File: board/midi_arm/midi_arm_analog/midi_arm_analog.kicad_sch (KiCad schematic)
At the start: 8 parts, among them U1 LM741

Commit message: analog sim update
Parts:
- R1, R3, R4, R5: value 1500 -> 2400
- R2: value 3900 -> 24000
- R_sense1: value 1400 -> 2400
- U1: value LM741 -> MCP6001
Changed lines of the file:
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@@
       (effects (font (size 1.27 1.27)) (justify left))
     )
-    (property "Value" "1400" (at 113.538 77.4121 0)
+    (property "Value" "2400" (at 113.538 77.4121 0)
       (effects (font (size 1.27 1.27)) (justify left))
     )
@@
       (effects (font (size 1.27 1.27)))
     )
-    (property "Value" "LM741" (at 152.7712 66.733 0)
+    (property "Value" "MCP6001" (at 152.7712 66.733 0)
       (effects (font (size 1.27 1.27)))
     )
@@
       (effects (font (size 1.27 1.27)) hide)
     )
-    (property "Sim.Library" "lm741.lib" (at 143.764 68.326 0)
-      (effects (font (size 1.27 1.27)) hide)
-    )
-    (property "Sim.Name" "LM741" (at 143.764 68.326 0)
+    (property "Sim.Library" "MCP6001.lib" (at 143.764 68.326 0)
+      (effects (font (size 1.27 1.27)) hide)
+    )
+    (property "Sim.Name" "MCP6001" (at 143.764 68.326 0)
       (effects (font (size 1.27 1.27)) hide)
     )
@@
       (effects (font (size 1.27 1.27)) hide)
     )
-    (property "Sim.Pins" "2=2 3=1 4=50 6=28 7=99" (at 143.764 68.326 0)
+    (property "Sim.Pins" "2=2 3=1 4=4 6=5 7=3" (at 143.764 68.326 0)
       (effects (font (size 1.27 1.27)) hide)
     )
@@
   (symbol (lib_id "Device:R") (at 127 82.804 90) (unit 1)
     (in_bom yes) (on_board yes) (dnp no) (fields_autoplaced)
-    (property "Reference" "R1" (at 127 77.6437 90)
-      (effects (font (size 1.27 1.27)))
-    )
-    (property "Value" "1500" (at 127 80.0679 90)
+    (property "Reference" "R1" (at 127 77.47 90)
+      (effects (font (size 1.27 1.27)))
+    )
+    (property "Value" "2400" (at 127 80.01 90)
       (effects (font (size 1.27 1.27)))
     )
@@
   (symbol (lib_id "Device:R") (at 136.144 82.804 90) (unit 1)
     (in_bom yes) (on_board yes) (dnp no) (fields_autoplaced)
-    (property "Reference" "R2" (at 136.144 77.6437 90)
-      (effects (font (size 1.27 1.27)))
-    )
-    (property "Value" "3900" (at 136.144 80.0679 90)
+    (property "Reference" "R2" (at 136.144 77.47 90)
+      (effects (font (size 1.27 1.27)))
+    )
+    (property "Value" "24000" (at 136.144 80.01 90)
       (effects (font (size 1.27 1.27)))
     )
@@
   (symbol (lib_id "Device:R") (at 101.6 66.04 0) (unit 1)
     (in_bom yes) (on_board yes) (dnp no) (fields_autoplaced)
-    (property "Reference" "R4" (at 103.378 64.8279 0)
-      (effects (font (size 1.27 1.27)) (justify left))
-    )
-    (property "Value" "1500" (at 103.378 67.2521 0)
+    (property "Reference" "R4" (at 104.14 64.77 0)
+      (effects (font (size 1.27 1.27)) (justify left))
+    )
+    (property "Value" "2400" (at 104.14 67.31 0)
       (effects (font (size 1.27 1.27)) (justify left))
     )
@@
   (symbol (lib_id "Device:R") (at 101.6 76.2 0) (unit 1)
     (in_bom yes) (on_board yes) (dnp no) (fields_autoplaced)
-    (property "Reference" "R5" (at 103.378 74.9879 0)
-      (effects (font (size 1.27 1.27)) (justify left))
-    )
-    (property "Value" "1500" (at 103.378 77.4121 0)
+    (property "Reference" "R5" (at 104.14 74.93 0)
+      (effects (font (size 1.27 1.27)) (justify left))
+    )
+    (property "Value" "2400" (at 104.14 77.47 0)
       (effects (font (size 1.27 1.27)) (justify left))
     )
@@
   (symbol (lib_id "Device:R") (at 111.76 66.04 0) (unit 1)
     (in_bom yes) (on_board yes) (dnp no) (fields_autoplaced)
-    (property "Reference" "R3" (at 113.538 64.8279 0)
-      (effects (font (size 1.27 1.27)) (justify left))
-    )
-    (property "Value" "1500" (at 113.538 67.2521 0)
-      (effects (font (size 1.27 1.27)) (justify left))
-    )
+    (property "Reference" "R3" (at 114.3 64.77 0)
+      (effects (font (size 1.27 1.27)) (justify left))
+    )
+    (property "Value" "2400" (at 114.3 67.31 0)
+      (effects (font (size 1.27 1.27)) (justify left))
+    )

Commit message: updates
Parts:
- R1, R5: value 2400 -> 3300
- R3: value 2400 -> 5100
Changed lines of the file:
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@@
   (symbol (lib_id "Device:R") (at 127 82.804 90) (unit 1)
     (in_bom yes) (on_board yes) (dnp no) (fields_autoplaced)
-    (property "Reference" "R1" (at 127 77.47 90)
+    (property "Reference" "R1" (at 127 77.6437 90)
       (effects (font (size 1.27 1.27)))
     )
-    (property "Value" "2400" (at 127 80.01 90)
+    (property "Value" "3300" (at 127 80.0679 90)
       (effects (font (size 1.27 1.27)))
     )
@@
   (symbol (lib_id "Device:R") (at 136.144 82.804 90) (unit 1)
     (in_bom yes) (on_board yes) (dnp no) (fields_autoplaced)
-    (property "Reference" "R2" (at 136.144 77.47 90)
+    (property "Reference" "R2" (at 136.144 77.6437 90)
       (effects (font (size 1.27 1.27)))
     )
-    (property "Value" "24000" (at 136.144 80.01 90)
+    (property "Value" "24000" (at 136.144 80.0679 90)
       (effects (font (size 1.27 1.27)))
     )
@@
   (symbol (lib_id "Device:R") (at 101.6 66.04 0) (unit 1)
     (in_bom yes) (on_board yes) (dnp no) (fields_autoplaced)
-    (property "Reference" "R4" (at 104.14 64.77 0)
+    (property "Reference" "R4" (at 103.378 64.8279 0)
       (effects (font (size 1.27 1.27)) (justify left))
     )
-    (property "Value" "2400" (at 104.14 67.31 0)
+    (property "Value" "2400" (at 103.378 67.2521 0)
       (effects (font (size 1.27 1.27)) (justify left))
     )
@@
   (symbol (lib_id "Device:R") (at 101.6 76.2 0) (unit 1)
     (in_bom yes) (on_board yes) (dnp no) (fields_autoplaced)
-    (property "Reference" "R5" (at 104.14 74.93 0)
+    (property "Reference" "R5" (at 103.378 74.9879 0)
       (effects (font (size 1.27 1.27)) (justify left))
     )
-    (property "Value" "2400" (at 104.14 77.47 0)
+    (property "Value" "3300" (at 103.378 77.4121 0)
       (effects (font (size 1.27 1.27)) (justify left))
     )
@@
   (symbol (lib_id "Device:R") (at 111.76 66.04 0) (unit 1)
     (in_bom yes) (on_board yes) (dnp no) (fields_autoplaced)
-    (property "Reference" "R3" (at 114.3 64.77 0)
+    (property "Reference" "R3" (at 113.538 64.8279 0)
       (effects (font (size 1.27 1.27)) (justify left))
     )
-    (property "Value" "2400" (at 114.3 67.31 0)
+    (property "Value" "5100" (at 113.538 67.2521 0)
       (effects (font (size 1.27 1.27)) (justify left))
     )

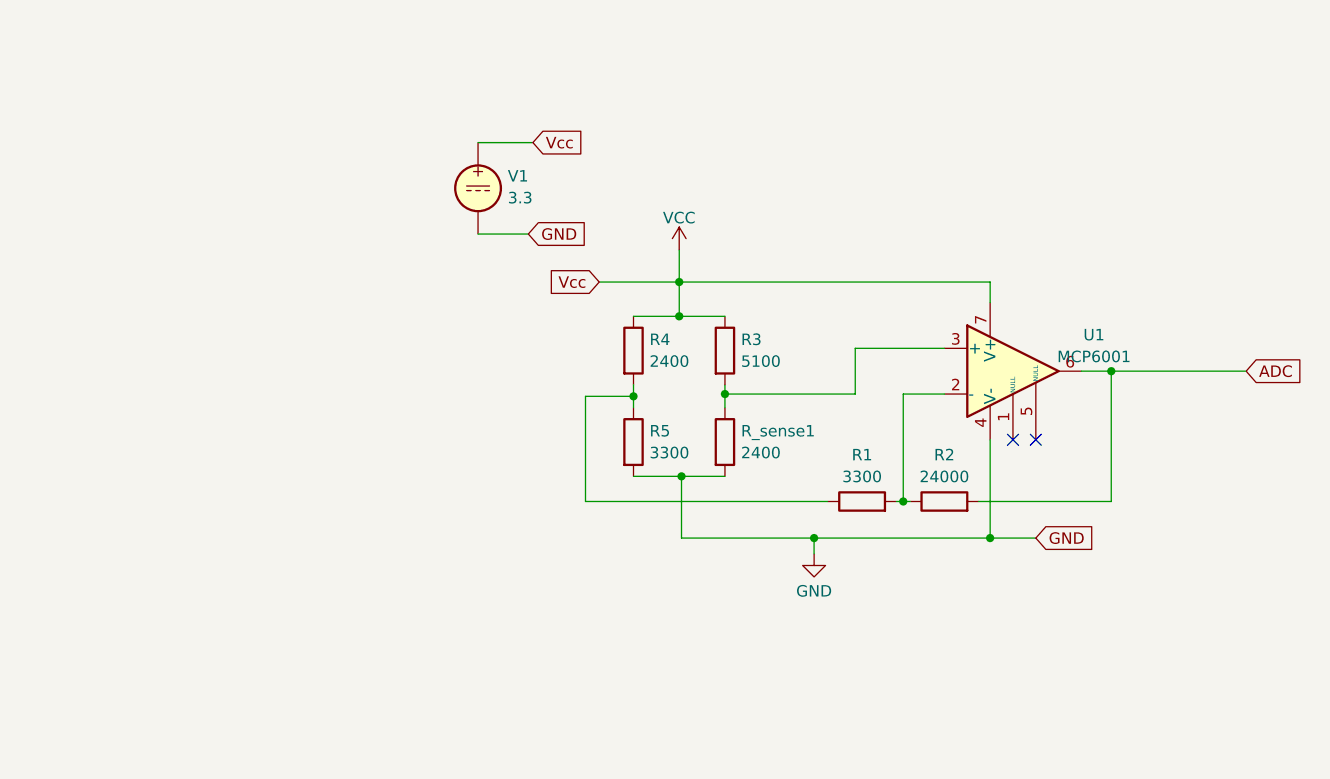
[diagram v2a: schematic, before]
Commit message: HW Version 3 Support
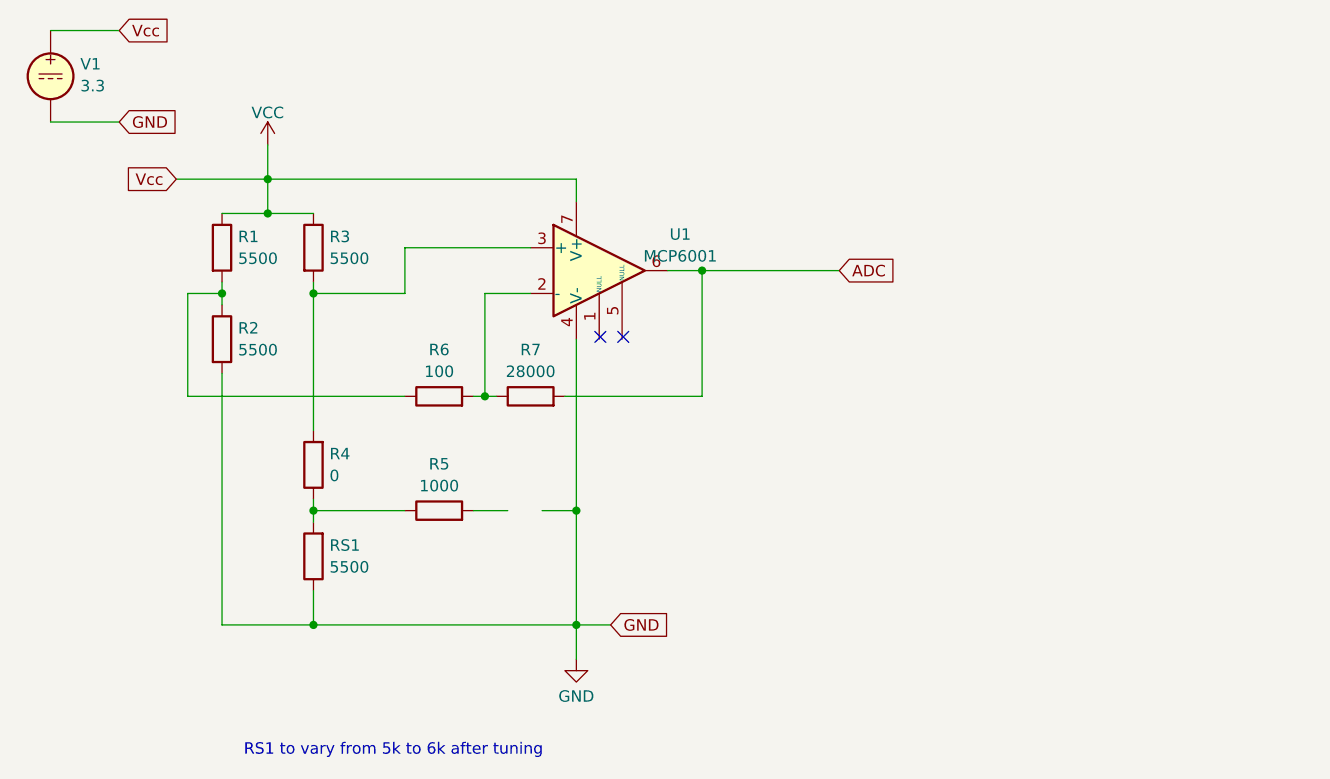
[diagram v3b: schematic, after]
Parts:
- removed R_sense1: 2400, symbol Device:R
- added R4: 0, symbol Device:R
- added R5: 1000, symbol Device:R
- added RS1: 5500, symbol Device:R
- R1: renamed from R4; value 2400 -> 5500
- R2: renamed from R5; value 3300 -> 5500
- R3: value 5100 -> 5500
- R6: renamed from R1; value 3300 -> 100
- R7: renamed from R2; value 24000 -> 28000
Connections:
- net GND: now also RS1.1
- net at R3.2, U1.3 (+): now also R4.2
- new net: R4.1, R5.1, RS1.2
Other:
- note added: "RS1 to vary from 5k to 6k after tuning"
- moved on the sheet: R1, R2, R3, R6, R7, U1, V1

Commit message: Bugfixes
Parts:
- R1, R2, R3: value 5500 -> 33000
- R4: value 0 -> 10000
- R5: value 1000 -> 0
- R6: value 100 -> 0
- R7: value 28000 -> 51000
- RS1: value 5500 -> 15000
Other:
- note added: "RS1 to vary from 10k to 20k after tuning -> Voltage output = 0-1.3V"
- note removed: "RS1 to vary from 5k to 6k after tuning"
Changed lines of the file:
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@@
-	)
-	(junction
-		(at 95.25 83.82)
-		(diameter 0)
-		(color 0 0 0 0)
 	)
 	(junction
@@
 	(wire
 		(pts
-			(xy 83.82 83.82) (xy 87.63 83.82)
-		)
-		(stroke
-			(width 0)
-			(type default)
-		)
-	)
-	(wire
-		(pts
 			(xy 52.07 71.12) (xy 76.2 71.12)
 		)
@@
 	(wire
 		(pts
-			(xy 95.25 83.82) (xy 95.25 96.52)
-		)
-		(stroke
-			(width 0)
-			(type default)
-		)
-	)
-	(wire
-		(pts
 			(xy 109.22 57.15) (xy 124.46 57.15)
 		)
@@
 	(wire
 		(pts
-			(xy 91.44 83.82) (xy 95.25 83.82)
-		)
-		(stroke
-			(width 0)
-			(type default)
-		)
-	)
-	(wire
-		(pts
 			(xy 55.88 96.52) (xy 66.04 96.52)
 		)
@@
 	(wire
 		(pts
-			(xy 95.25 64.77) (xy 95.25 83.82)
+			(xy 95.25 64.77) (xy 95.25 96.52)
 		)
 		(stroke
@@
 		)
 	)
-	(text "RS1 to vary from 5k to 6k after tuning"
+	(text "RS1 to vary from 10k to 20k after tuning -> Voltage output = 0-1.3V"
 		(exclude_from_sim no)
 		(at 74.93 110.49 0)
@@
 			)
 		)
-		(property "Value" "1000"
+		(property "Value" "0"
 			(at 80.01 81.0838 90)
 			(effects
@@
 			)
 		)
-		(property "Value" "100"
+		(property "Value" "0"
 			(at 80.01 68.3838 90)
 			(effects
@@
 			)
 		)
-		(property "Value" "0"
+		(property "Value" "10000"
 			(at 67.818 79.9521 0)
 			(effects
@@
 			)
 		)
-		(property "Value" "28000"
+		(property "Value" "51000"
 			(at 90.17 68.3838 90)
 			(effects
@@
 			)
 		)
-		(property "Value" "5500"
+		(property "Value" "33000"
 			(at 57.658 55.8221 0)
 			(effects
@@
 			)
 		)
-		(property "Value" "5500"
+		(property "Value" "15000"
 			(at 67.818 90.1121 0)
 			(effects
@@
 			)
 		)
-		(property "Value" "5500"
+		(property "Value" "33000"
 			(at 57.658 65.9821 0)
 			(effects
@@
 			)
 		)
-		(property "Value" "5500"
+		(property "Value" "33000"
 			(at 67.818 55.8221 0)
 			(effects

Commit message: Board 3.5 and code cleanup
Mini version of Baboi
Remove Tension Strip option 3/4
Remove  Option for Touch pads
Move light control to host software
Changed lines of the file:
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@@
 		(fields_autoplaced yes)
 		(property "Reference" "V1"
-			(at 40.132 34.2181 0)
+			(at 40.132 34.218 0)
 			(effects
 				(font

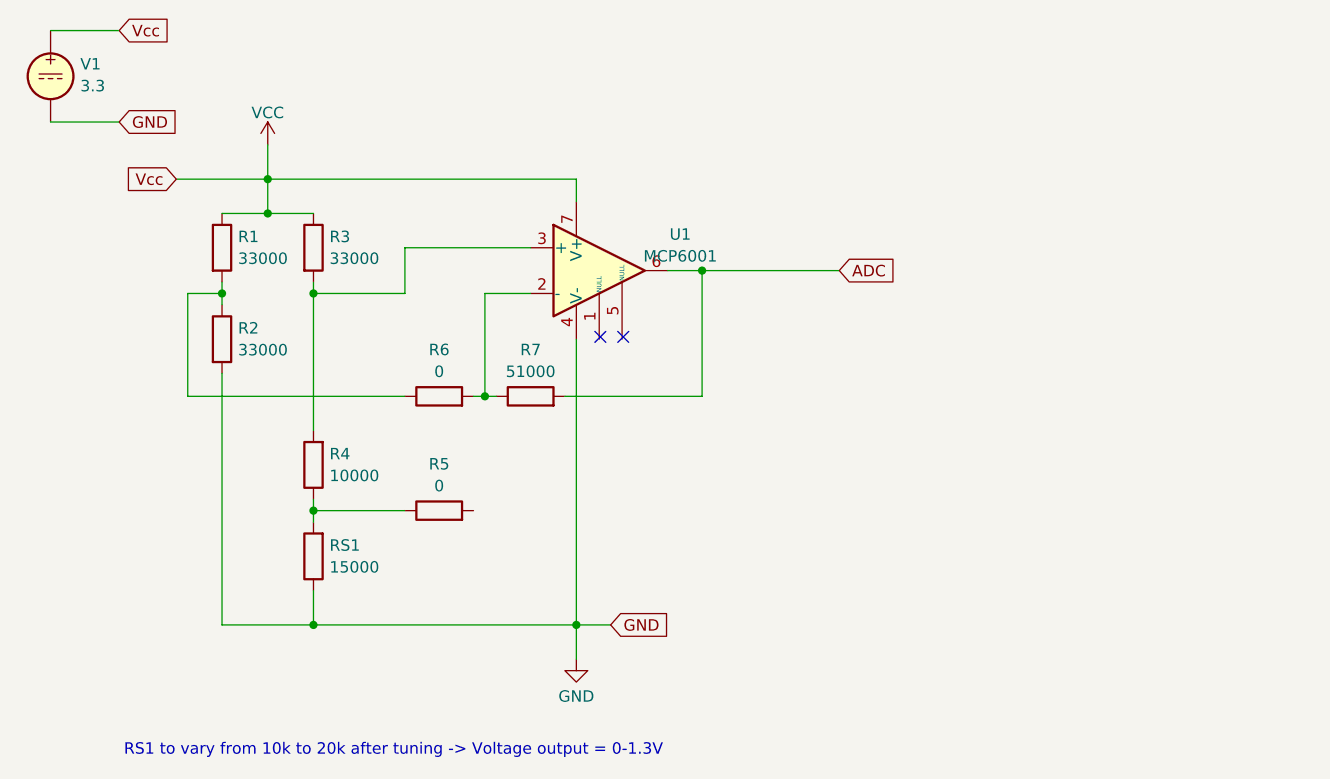
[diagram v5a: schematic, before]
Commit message: Add Led FX, absolute direction calibration, Arrow 3D
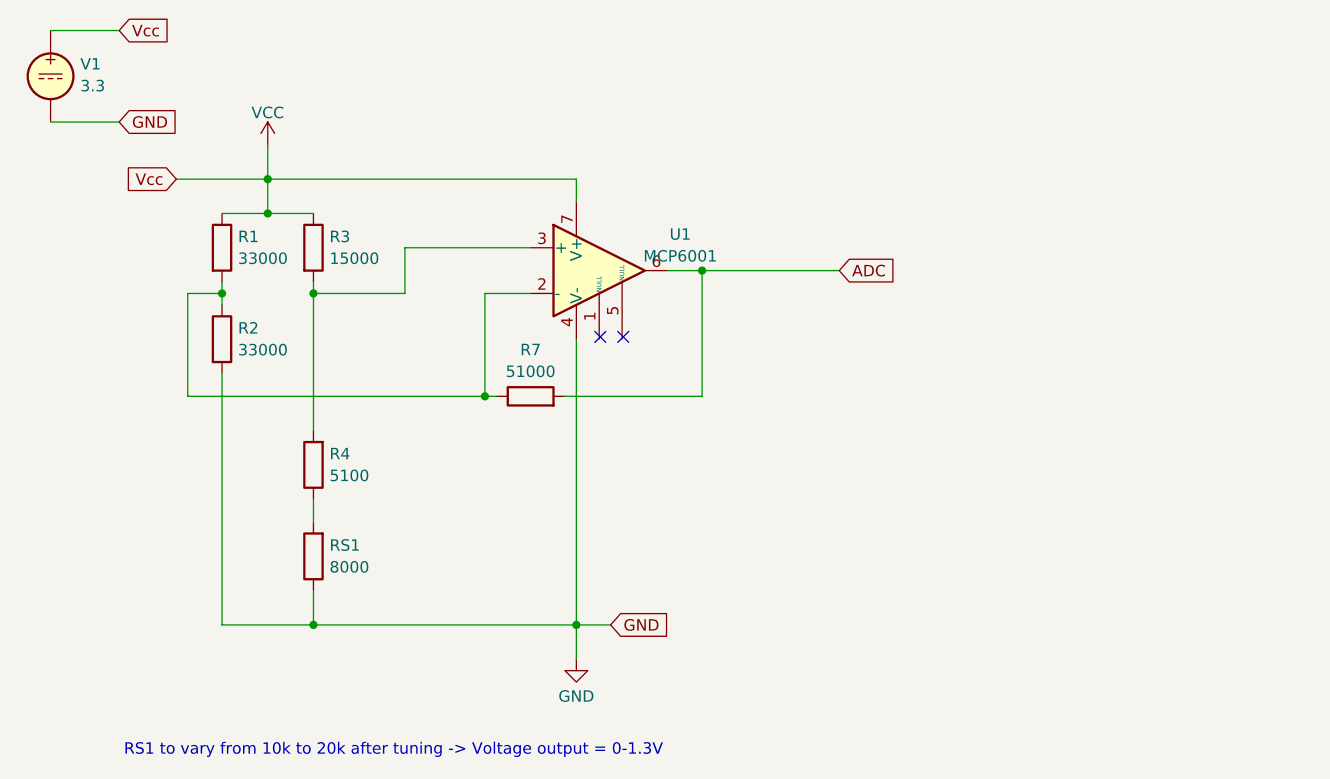
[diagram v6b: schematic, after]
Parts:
- removed R5, R6: 0, symbol Device:R
- R3: value 33000 -> 15000
- R4: value 10000 -> 5100
- RS1: value 15000 -> 8000
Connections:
- net at R7.1, U1.2 (-): now also R1.2, R2.1
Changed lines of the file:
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@@
-	)
-	(junction
-		(at 66.04 83.82)
-		(diameter 0)
-		(color 0 0 0 0)
 	)
 	(junction
@@
 	(wire
 		(pts
-			(xy 52.07 71.12) (xy 76.2 71.12)
+			(xy 52.07 71.12) (xy 85.09 71.12)
 		)
 		(stroke
@@
 	(wire
 		(pts
-			(xy 83.82 71.12) (xy 85.09 71.12)
-		)
-		(stroke
-			(width 0)
-			(type default)
-		)
-	)
-	(wire
-		(pts
 			(xy 109.22 57.15) (xy 124.46 57.15)
 		)
@@
 	(wire
 		(pts
-			(xy 66.04 82.55) (xy 66.04 83.82)
-		)
-		(stroke
-			(width 0)
-			(type default)
-		)
-	)
-	(wire
-		(pts
 			(xy 95.25 64.77) (xy 95.25 96.52)
 		)
@@
 	(wire
 		(pts
-			(xy 66.04 83.82) (xy 76.2 83.82)
-		)
-		(stroke
-			(width 0)
-			(type default)
-		)
-	)
-	(wire
-		(pts
 			(xy 60.96 46.99) (xy 60.96 50.8)
 		)
@@
 	(wire
 		(pts
-			(xy 66.04 83.82) (xy 66.04 85.09)
+			(xy 66.04 82.55) (xy 66.04 85.09)
 		)
 		(stroke
@@
 	)
 	(symbol
-		(lib_id "Device:R")
-		(at 80.01 83.82 90)
-		(unit 1)
-		(exclude_from_sim no)
-		(in_bom yes)
-		(on_board yes)
-		(dnp no)
-		(fields_autoplaced yes)
-		(property "Reference" "R5"
-			(at 80.01 78.6595 90)
-			(effects
-				(font
-					(size 1.27 1.27)
-				)
-			)
-		)
-		(property "Value" "0"
-			(at 80.01 81.0838 90)
-			(effects
-				(font
-					(size 1.27 1.27)
-				)
-			)
-		)
-		(property "Footprint" ""
-			(at 80.01 85.598 90)
-			(effects
-				(font
-					(size 1.27 1.27)
-				)
-				(hide yes)
-			)
-		)
-		(property "Datasheet" "~"
-			(at 80.01 83.82 0)
-			(effects
-				(font
-					(size 1.27 1.27)
-				)
-				(hide yes)
-			)
-		)
-		(property "Description" ""
-			(at 80.01 83.82 0)
-			(effects
-				(font
-					(size 1.27 1.27)
-				)
-				(hide yes)
-			)
-		)
-		(pin "1"
-		)
-		(pin "2"
-		)
-		(instances
-			(project "midi_arm_analog"
-				(path "/307ce423-bb1b-4eb8-9c81-09800713e2e7"
-					(reference "R5")
-					(unit 1)
-				)
-			)
-		)
-	)
-	(symbol
 		(lib_id "Amplifier_Operational:LM741")
 		(at 97.79 57.15 0)
@@
 				(path "/307ce423-bb1b-4eb8-9c81-09800713e2e7"
 					(reference "U1")
-					(unit 1)
-				)
-			)
-		)
-	)
-	(symbol
-		(lib_id "Device:R")
-		(at 80.01 71.12 90)
-		(unit 1)
-		(exclude_from_sim no)
-		(in_bom yes)
-		(on_board yes)
-		(dnp no)
-		(fields_autoplaced yes)
-		(property "Reference" "R6"
-			(at 80.01 65.9595 90)
-			(effects
-				(font
-					(size 1.27 1.27)
-				)
-			)
-		)
-		(property "Value" "0"
-			(at 80.01 68.3838 90)
-			(effects
-				(font
-					(size 1.27 1.27)
-				)
-			)
-		)
-		(property "Footprint" ""
-			(at 80.01 72.898 90)
-			(effects
-				(font
-					(size 1.27 1.27)
-				)
-				(hide yes)
-			)
-		)
-		(property "Datasheet" "~"
-			(at 80.01 71.12 0)
-			(effects
-				(font
-					(size 1.27 1.27)
-				)
-				(hide yes)
-			)
-		)
-		(property "Description" ""
-			(at 80.01 71.12 0)
-			(effects
-				(font
-					(size 1.27 1.27)
-				)
-				(hide yes)
-			)
-		)
-		(pin "1"
-		)
-		(pin "2"
-		)
-		(instances
-			(project "midi_arm_analog"
-				(path "/307ce423-bb1b-4eb8-9c81-09800713e2e7"
-					(reference "R6")
 					(unit 1)
 				)
@@
 			)
 		)
-		(property "Value" "10000"
+		(property "Value" "5100"
 			(at 67.818 79.9521 0)
 			(effects
@@
 			)
 		)
-		(property "Value" "15000"
+		(property "Value" "8000"
 			(at 67.818 90.1121 0)
 			(effects
@@
 			)
 		)
-		(property "Value" "33000"
+		(property "Value" "15000"
 			(at 67.818 55.8221 0)
 			(effects

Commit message: minor bug fixes
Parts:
- R3: value 15000 -> 33000
- R4: value 5100 -> 15000
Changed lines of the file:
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@@
 			)
 		)
-		(property "Value" "5100"
+		(property "Value" "15000"
 			(at 67.818 79.9521 0)
 			(effects
@@
 			)
 		)
-		(property "Value" "15000"
+		(property "Value" "33000"
 			(at 67.818 55.8221 0)
 			(effects
